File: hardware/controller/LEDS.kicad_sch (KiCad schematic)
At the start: 24 parts, among them IC2 PCA9685PW_Q900,118

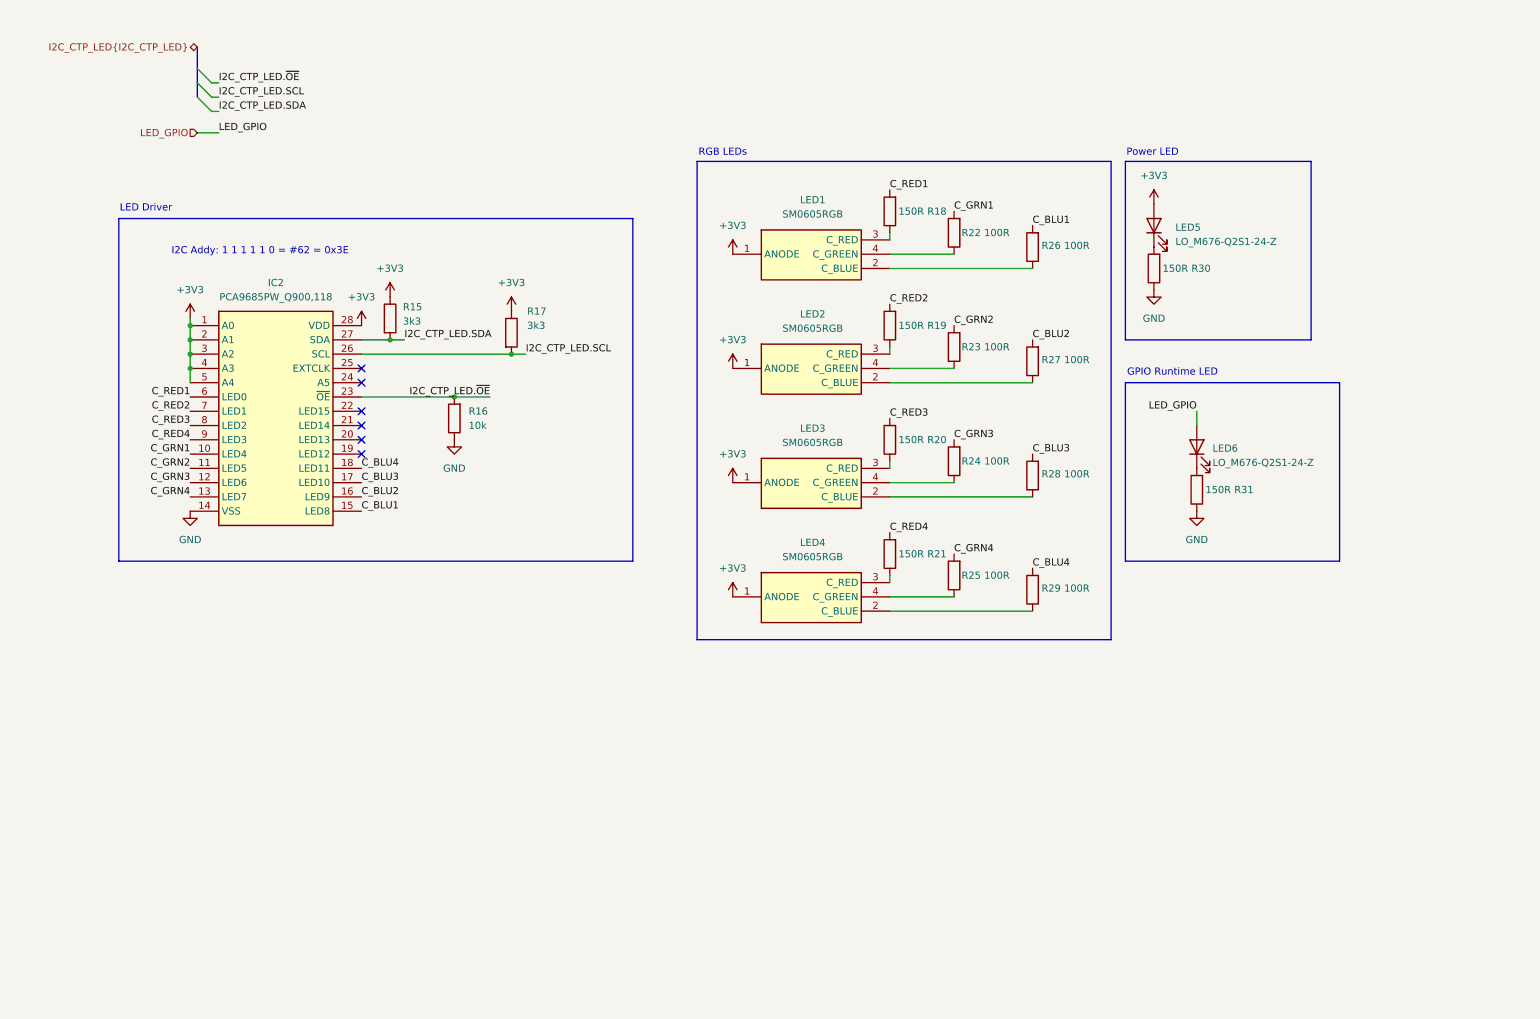
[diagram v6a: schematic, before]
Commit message: Moved LEDs around. Replaced some discrete resistors with resistor arrays. Added mounting holes. Added. Added a lot of actual components for passive elements
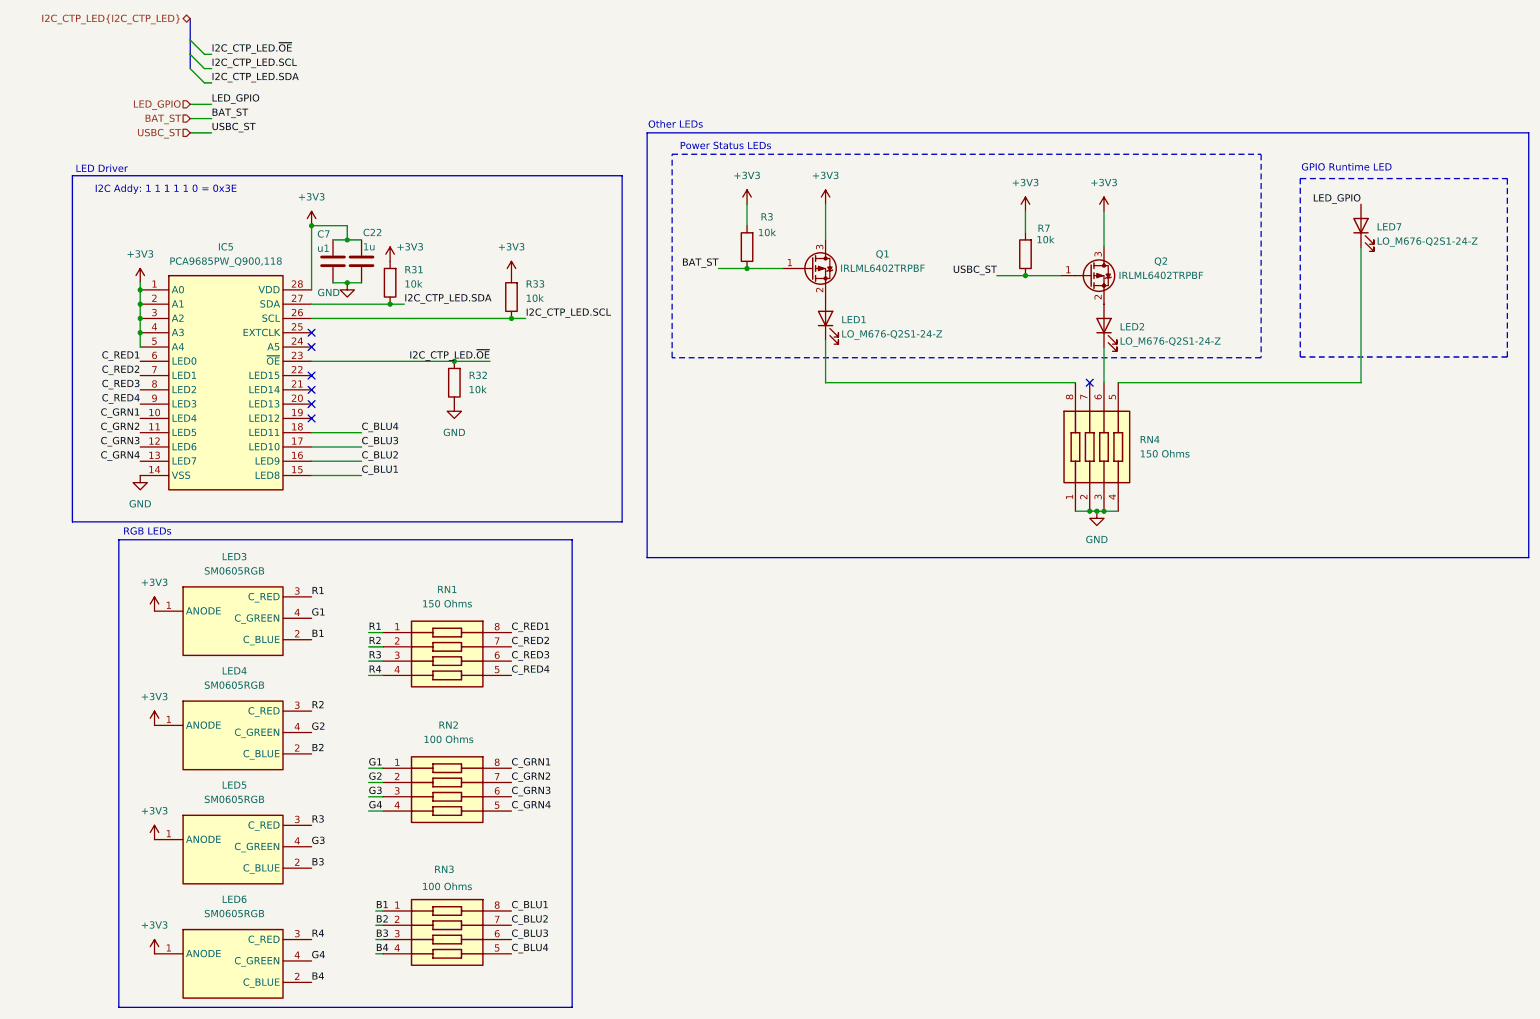
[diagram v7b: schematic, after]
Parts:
- removed LED5: LO_M676-Q2S1-24-Z, SamacSys_Parts:LEDM2214X140N, symbol Device:LED
- removed R15, R17: 3k3, symbol Device:R
- removed R18, R19, R20, R21, R30: 150R, SamacSys_Parts:RESC2012X60N, symbol Device:R
- removed R22, R23, R24, R25, R26, R27, R28, R29: 100R, SamacSys_Parts:RESC2012X65N, symbol Device:R
- added C22: 1u, CAPC2012X135N, symbol Device:C
- added C7: u1, MAJx16, symbol Device:C
- added LED1, LED2: LO_M676-Q2S1-24-Z, SamacSys_Parts:LEDM2214X140N, symbol Device:LED
- added Q1, Q2: IRLML6402TRPBF, Package_TO_SOT_SMD:SOT-23, symbol Transistor_FET:IRLML6402
- added R3, R33, R7: 10k, RESC2012X60N, symbol Device:R
- added RN1, RN4: 150 Ohms, EXBV8V151JV, symbol SamacSys_Parts:EXB-V8V151JV
- added RN2, RN3: 100 Ohms, EXBU38, symbol SamacSys_Parts:EXB-U38101JV
- IC5: renamed from IC2; footprint SamacSys_Parts:SOP65P640X110-28N -> SOP65P640X110-28N
- LED3: renamed from LED1; footprint SamacSys_Parts:SM0605RGB -> SM0605RGB
- LED4: renamed from LED2; footprint SamacSys_Parts:SM0605RGB -> SM0605RGB
- LED5: renamed from LED3; footprint SamacSys_Parts:SM0605RGB -> SM0605RGB
- LED6: renamed from LED4; footprint SamacSys_Parts:SM0605RGB -> SM0605RGB
- R31: value 150R -> 10k; footprint SamacSys_Parts:RESC2012X60N -> RESC2012X60N; Height (none) -> 0.6; Manufacturer_Name KOA Speer -> TT Electronics; Manufacturer_Part_Number RK73B2ATTD151J -> ASC0805-10KFT5; Mouser Part Number 660-RK73B2ATTD151J -> 756-ASC0805-10KFT5; Mouser Price/Stock https://www.mouser.co.uk/ProductDetail/KOA-Speer/RK73B2ATTD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 -> https://www.mouser.co.uk/ProductDetail/Welwyn-Components-TT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
- R32: renamed from R16; footprint (none) -> RESC2012X60N; Height (none) -> 0.6; Manufacturer_Name (none) -> TT Electronics; Manufacturer_Part_Number (none) -> ASC0805-10KFT5; Mouser Part Number (none) -> 756-ASC0805-10KFT5; Mouser Price/Stock (none) -> https://www.mouser.co.uk/ProductDetail/Welwyn-Components-TT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
- renumbered LED6 to LED7
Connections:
- net +3V3: now also R31.2, C22.1, C7.1, Q1.3 (D), Q2.3 (D), R3.2, R33.2, R7.2
- net C_BLU1: now also RN3.8
- net C_BLU2: now also RN3.7
- net C_BLU3: now also RN3.6
- net C_BLU4: now also RN3.5
- net C_GRN1: now also RN2.8
- net C_GRN2: now also RN2.7
- net C_GRN3: now also RN2.6
- net C_GRN4: now also RN2.5
- net C_RED1: now also RN1.8
- net C_RED2: now also RN1.7
- net C_RED3: now also RN1.6
- net C_RED4: now also RN1.5
- net GND: now also C22.2, C7.2, RN4.1, RN4.2, RN4.3, RN4.4; no longer R31.1
- net I2C_CTP_LED.SCL: now also R33.1
- net I2C_CTP_LED.SDA: now also R31.1
- net B3: now reaches LED5.2 (C_BLUE)
- net B3: now also RN3.3
- net R3: now reaches LED5.3 (C_RED)
- net R3: now also RN1.3
- net G3: now reaches LED5.4 (C_GREEN)
- net G3: now also RN2.3
- net G4: now reaches LED6.4 (C_GREEN)
- net G4: now also RN2.4
- net B1: now reaches LED3.2 (C_BLUE)
- net B1: now also RN3.1
- net R1: now reaches LED3.3 (C_RED)
- net R1: now also RN1.1
- net G1: now reaches LED3.4 (C_GREEN)
- net G1: now also RN2.1
- net B4: now reaches LED6.2 (C_BLUE)
- net B4: now also RN3.4
- net R4: now reaches LED6.3 (C_RED)
- net R4: now also RN1.4
- net B2: now reaches LED4.2 (C_BLUE)
- net B2: now also RN3.2
- net R2: now reaches LED4.3 (C_RED)
- net R2: now also RN1.2
- net G2: now reaches LED4.4 (C_GREEN)
- net G2: now also RN2.2
- net at LED7.1 (K): now also RN4.5; no longer R31.2
- new net: LED2.2 (A), Q2.2 (S)
- new net: LED2.1 (K), RN4.6
- new net: LED1.2 (A), Q1.2 (S)
- new net: LED1.1 (K), RN4.8
- new net BAT_ST: Q1.1 (G), R3.1
- new net USBC_ST: Q2.1 (G), R7.1
- no-connect marks 6 -> 7
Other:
- note added: "I2C Addy: 1 1 1 1 1 0 = 0x3E"
- note added: "Other LEDs"
- note added: "Power Status LEDs"
- note removed: "I2C Addy: 1 1 1 1 1 0 = #62 = 0x3E"
- note removed: "Power LED"
- moved on the sheet: IC5, LED3, LED4, LED5, LED6, LED7, R32

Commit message: ERC good to go. grouped all components on pcb
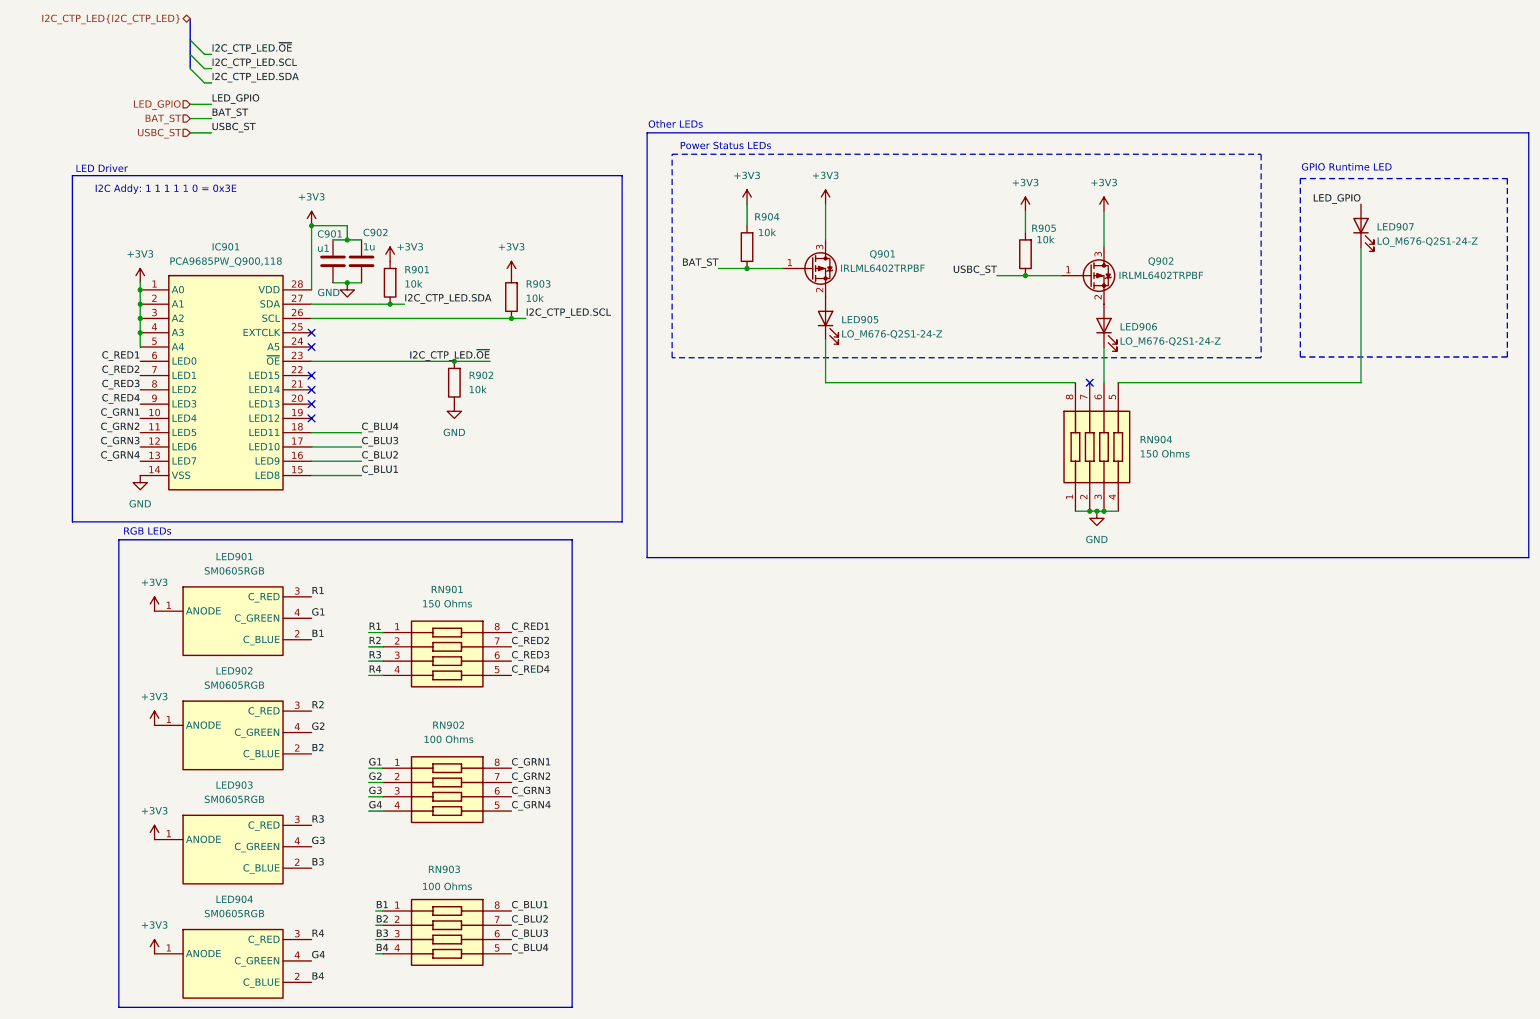
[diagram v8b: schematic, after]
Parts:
- C901: renamed from C7; footprint MAJx16 -> SamacSys_Parts:MAJx16
- C902: renamed from C22; footprint CAPC2012X135N -> SamacSys_Parts:CAPC2012X135N
- IC901: renamed from IC5; footprint SOP65P640X110-28N -> SamacSys_Parts:SOP65P640X110-28N
- LED901: renamed from LED3; footprint SM0605RGB -> SamacSys_Parts:SM0605RGB
- LED902: renamed from LED4; footprint SM0605RGB -> SamacSys_Parts:SM0605RGB
- LED903: renamed from LED5; footprint SM0605RGB -> SamacSys_Parts:SM0605RGB
- LED904: renamed from LED6; footprint SM0605RGB -> SamacSys_Parts:SM0605RGB
- R901: renamed from R31; footprint RESC2012X60N -> SamacSys_Parts:RESC2012X60N
- R902: renamed from R32; footprint RESC2012X60N -> SamacSys_Parts:RESC2012X60N
- R903: renamed from R33; footprint RESC2012X60N -> SamacSys_Parts:RESC2012X60N
- R904: renamed from R3; footprint RESC2012X60N -> SamacSys_Parts:RESC2012X60N
- R905: renamed from R7; footprint RESC2012X60N -> SamacSys_Parts:RESC2012X60N
- RN901: renamed from RN1; footprint EXBV8V151JV -> SamacSys_Parts:EXBV8V151JV
- RN902: renamed from RN2; footprint EXBU38 -> SamacSys_Parts:EXBU38
- RN903: renamed from RN3; footprint EXBU38 -> SamacSys_Parts:EXBU38
- RN904: renamed from RN4; footprint EXBV8V151JV -> SamacSys_Parts:EXBV8V151JV
- renumbered LED1 to LED905, LED2 to LED906, LED7 to LED907, Q1 to Q901, Q2 to Q902
